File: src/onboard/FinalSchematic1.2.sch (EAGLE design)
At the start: 81 parts, among them IC1 MIC29310-5.0BT, IC3 A5975D

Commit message: Removed old baro
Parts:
- removed BAROMETER: (no value), con-lstb:MA04-1
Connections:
- net 5V: no longer BAROMETER.1
- net GND: no longer BAROMETER.2
- net SCL: no longer BAROMETER.4
- net SDA: no longer BAROMETER.3
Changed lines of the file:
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@@
 <part name="GPSMTK3339" library="AERO_Eagle_Library" deviceset="ADAFRUIT_MTK3339_GPS" device=""/>
 <part name="RADIO" library="AERO_Eagle_Library" deviceset="ADAFRUIT_RFM95W_LORA_RADIO" device=""/>
-<part name="BAROMETER" library="con-lstb" library_urn="urn:adsk.eagle:library:162" deviceset="MA04-1" device="" package3d_urn="urn:adsk.eagle:package:8337/1"/>
 <part name="SERVO_DRIVER" library="PCA9685PW_112" deviceset="PCA9685PW,112" device=""/>
 <part name="GND2" library="supply1" library_urn="urn:adsk.eagle:library:371" deviceset="GND" device=""/>
@@
 <instance part="GPSMTK3339" gate="G$1" x="48.26" y="80.01" smashed="yes" rot="R270"/>
 <instance part="RADIO" gate="G$1" x="96.52" y="78.74" smashed="yes" rot="R270"/>
-<instance part="BAROMETER" gate="1" x="-2.54" y="58.42" smashed="yes" rot="R180">
-<attribute name="VALUE" x="-1.27" y="68.58" size="1.778" layer="96" rot="R180"/>
-<attribute name="NAME" x="-1.27" y="52.578" size="1.778" layer="95" rot="R180"/>
-</instance>
 <instance part="IMU" gate="G$1" x="144.78" y="35.56" smashed="yes" rot="R270"/>
 <instance part="R32" gate="G$1" x="76.2" y="5.08" smashed="yes" rot="R90">
@@
 </segment>
 <segment>
-<pinref part="BAROMETER" gate="1" pin="1"/>
-<wire x1="-10.16" y1="63.5" x2="-12.7" y2="63.5" width="0.1524" layer="91"/>
-<label x="-17.78" y="63.5" size="1.778" layer="95"/>
-</segment>
-<segment>
 <pinref part="RADIO" gate="G$1" pin="VIN"/>
 <wire x1="91.44" y1="73.66" x2="87.63" y2="73.66" width="0.1524" layer="91"/>
@@
 </segment>
 <segment>
-<pinref part="BAROMETER" gate="1" pin="3"/>
-<wire x1="-10.16" y1="58.42" x2="-12.7" y2="58.42" width="0.1524" layer="91"/>
-<label x="-17.78" y="58.42" size="1.778" layer="95"/>
-</segment>
-<segment>
 <pinref part="R33" gate="G$1" pin="1"/>
 <wire x1="66.04" y1="0" x2="66.04" y2="-2.54" width="0.1524" layer="91"/>
@@
 </segment>
 <segment>
-<pinref part="BAROMETER" gate="1" pin="4"/>
-<wire x1="-10.16" y1="55.88" x2="-12.7" y2="55.88" width="0.1524" layer="91"/>
-<label x="-17.78" y="55.88" size="1.778" layer="95"/>
-</segment>
-<segment>
 <pinref part="R32" gate="G$1" pin="1"/>
 <wire x1="76.2" y1="0" x2="76.2" y2="-2.54" width="0.1524" layer="91"/>
@@
 </segment>
 <segment>
-<pinref part="BAROMETER" gate="1" pin="2"/>
-<wire x1="-10.16" y1="60.96" x2="-12.7" y2="60.96" width="0.1524" layer="91"/>
-<label x="-17.78" y="60.96" size="1.778" layer="95"/>
-</segment>
-<segment>

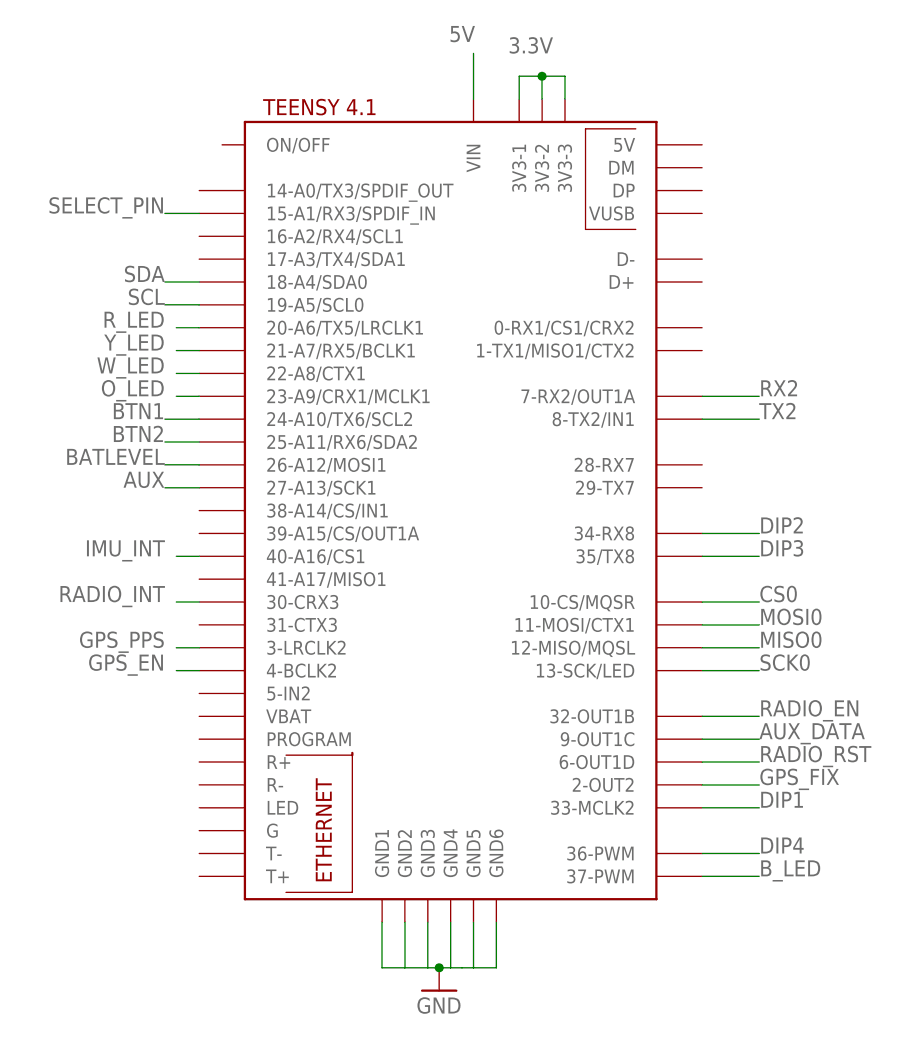
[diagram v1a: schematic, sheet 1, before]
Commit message: Rewired pins for easier routing
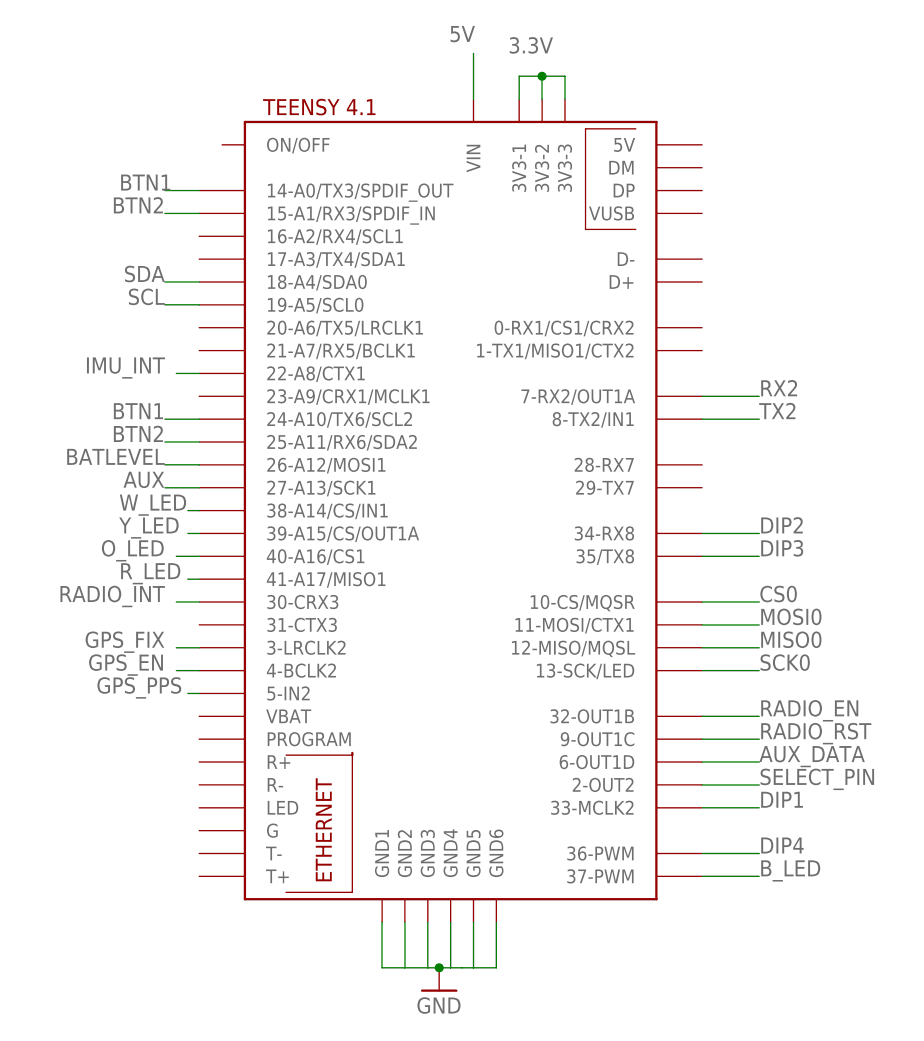
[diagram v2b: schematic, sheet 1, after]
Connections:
- net AUX_DATA: now also TEENSY4.1.6-OUT1D; no longer TEENSY4.1.9-OUT1C
- net BTN1: now also TEENSY4.1.14-A0/TX3/SPDIF_OUT
- net BTN2: now also TEENSY4.1.15-A1/RX3/SPDIF_IN
- net GPS_FIX: now also TEENSY4.1.3-LRCLK2; no longer TEENSY4.1.2-OUT2
- net GPS_PPS: now also TEENSY4.1.5-IN2; no longer TEENSY4.1.3-LRCLK2
- net IMU_INT: now also TEENSY4.1.22-A8/CTX1; no longer TEENSY4.1.40-A16/CS1
- net O_LED: now also TEENSY4.1.40-A16/CS1; no longer TEENSY4.1.23-A9/CRX1/MCLK1
- net RADIO_RST: now also TEENSY4.1.9-OUT1C; no longer TEENSY4.1.6-OUT1D
- net R_LED: now also TEENSY4.1.41-A17/MISO1; no longer TEENSY4.1.20-A6/TX5/LRCLK1
- net SELECT_PIN: now also TEENSY4.1.2-OUT2; no longer TEENSY4.1.15-A1/RX3/SPDIF_IN
- net W_LED: now also TEENSY4.1.38-A14/CS/IN1; no longer TEENSY4.1.22-A8/CTX1
- net Y_LED: now also TEENSY4.1.39-A15/CS/OUT1A; no longer TEENSY4.1.21-A7/RX5/BCLK1
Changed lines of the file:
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@@
-</segment>
-</net>
-<net name="GPS_FIX" class="0">
-<segment>
-<pinref part="TEENSY4.1" gate="G$1" pin="2-OUT2"/>
-<wire x1="90.17" y1="15.24" x2="96.52" y2="15.24" width="0.1524" layer="91"/>
-<label x="96.52" y="15.24" size="1.778" layer="95"/>
 </segment>
 </net>
 <net name="GPS_PPS" class="0">
 <segment>
-<pinref part="TEENSY4.1" gate="G$1" pin="3-LRCLK2"/>
-<wire x1="34.29" y1="30.48" x2="31.75" y2="30.48" width="0.1524" layer="91"/>
-<label x="30.48" y="30.48" size="1.778" layer="95" align="bottom-right"/>
+<pinref part="TEENSY4.1" gate="G$1" pin="5-IN2"/>
+<wire x1="34.29" y1="25.4" x2="33.02" y2="25.4" width="0.1524" layer="91"/>
+<label x="22.86" y="25.4" size="1.778" layer="95"/>
 </segment>
 </net>
@@
 <wire x1="34.29" y1="35.56" x2="31.75" y2="35.56" width="0.1524" layer="91"/>
 <label x="30.48" y="35.56" size="1.778" layer="95" align="bottom-right"/>
-</segment>
-</net>
-<net name="RADIO_RST" class="0">
-<segment>
-<pinref part="TEENSY4.1" gate="G$1" pin="6-OUT1D"/>
-<wire x1="90.17" y1="17.78" x2="96.52" y2="17.78" width="0.1524" layer="91"/>
-<label x="96.52" y="17.78" size="1.778" layer="95"/>
 </segment>
 </net>
@@
 <net name="IMU_INT" class="0">
 <segment>
-<pinref part="TEENSY4.1" gate="G$1" pin="40-A16/CS1"/>
-<wire x1="34.29" y1="40.64" x2="31.75" y2="40.64" width="0.1524" layer="91"/>
-<label x="30.48" y="40.64" size="1.778" layer="95" align="bottom-right"/>
-</segment>
-</net>
-<net name="W_LED" class="0">
-<segment>
 <pinref part="TEENSY4.1" gate="G$1" pin="22-A8/CTX1"/>
 <wire x1="34.29" y1="60.96" x2="31.75" y2="60.96" width="0.1524" layer="91"/>
 <label x="30.48" y="60.96" size="1.778" layer="95" align="bottom-right"/>
-</segment>
-</net>
-<net name="Y_LED" class="0">
-<segment>
-<pinref part="TEENSY4.1" gate="G$1" pin="21-A7/RX5/BCLK1"/>
-<wire x1="34.29" y1="63.5" x2="31.75" y2="63.5" width="0.1524" layer="91"/>
-<label x="30.48" y="63.5" size="1.778" layer="95" align="bottom-right"/>
-</segment>
-</net>
-<net name="R_LED" class="0">
-<segment>
-<pinref part="TEENSY4.1" gate="G$1" pin="20-A6/TX5/LRCLK1"/>
-<wire x1="34.29" y1="66.04" x2="31.75" y2="66.04" width="0.1524" layer="91"/>
-<label x="30.48" y="66.04" size="1.778" layer="95" align="bottom-right"/>
 </segment>
 </net>
@@
 <net name="AUX_DATA" class="0">
 <segment>
-<pinref part="TEENSY4.1" gate="G$1" pin="9-OUT1C"/>
-<wire x1="90.17" y1="20.32" x2="96.52" y2="20.32" width="0.1524" layer="91"/>
-<label x="96.52" y="20.32" size="1.778" layer="95"/>
-</segment>
-</net>
-<net name="SELECT_PIN" class="0">
-<segment>
-<pinref part="TEENSY4.1" gate="G$1" pin="15-A1/RX3/SPDIF_IN"/>
-<wire x1="34.29" y1="78.74" x2="30.48" y2="78.74" width="0.1524" layer="91"/>
-<label x="30.48" y="78.74" size="1.778" layer="95" align="bottom-right"/>
-</segment>
-</net>
-<net name="O_LED" class="0">
-<segment>
-<pinref part="TEENSY4.1" gate="G$1" pin="23-A9/CRX1/MCLK1"/>
-<wire x1="34.29" y1="58.42" x2="31.75" y2="58.42" width="0.1524" layer="91"/>
-<label x="30.48" y="58.42" size="1.778" layer="95" align="bottom-right"/>
+<pinref part="TEENSY4.1" gate="G$1" pin="6-OUT1D"/>
+<wire x1="90.17" y1="17.78" x2="96.52" y2="17.78" width="0.1524" layer="91"/>
+<label x="96.52" y="17.78" size="1.778" layer="95"/>
 </segment>
 </net>
@@
 <label x="30.48" y="53.34" size="1.778" layer="95" align="bottom-right"/>
 </segment>
+<segment>
+<pinref part="TEENSY4.1" gate="G$1" pin="15-A1/RX3/SPDIF_IN"/>
+<wire x1="34.29" y1="78.74" x2="30.48" y2="78.74" width="0.1524" layer="91"/>
+<label x="30.48" y="78.74" size="1.778" layer="95" align="bottom-right"/>
+</segment>
 </net>
 <net name="BTN1" class="0">
@@
 <wire x1="34.29" y1="55.88" x2="30.48" y2="55.88" width="0.1524" layer="91"/>
 <label x="30.48" y="55.88" size="1.778" layer="95" align="bottom-right"/>
+</segment>
+<segment>
+<pinref part="TEENSY4.1" gate="G$1" pin="14-A0/TX3/SPDIF_OUT"/>
+<wire x1="34.29" y1="81.28" x2="30.48" y2="81.28" width="0.1524" layer="91"/>
+<label x="25.4" y="81.28" size="1.778" layer="95"/>
 </segment>
 </net>
@@
 </segment>
 </net>
+<net name="RADIO_RST" class="0">
+<segment>
+<pinref part="TEENSY4.1" gate="G$1" pin="9-OUT1C"/>
+<wire x1="90.17" y1="20.32" x2="96.52" y2="20.32" width="0.1524" layer="91"/>
+<label x="96.52" y="20.32" size="1.778" layer="95"/>
+</segment>
+</net>
+<net name="W_LED" class="0">
+<segment>
+<pinref part="TEENSY4.1" gate="G$1" pin="38-A14/CS/IN1"/>
+<wire x1="34.29" y1="45.72" x2="33.02" y2="45.72" width="0.1524" layer="91"/>
+<label x="25.4" y="45.72" size="1.778" layer="95"/>
+</segment>
+</net>
+<net name="Y_LED" class="0">
+<segment>
+<pinref part="TEENSY4.1" gate="G$1" pin="39-A15/CS/OUT1A"/>
+<wire x1="34.29" y1="43.18" x2="33.02" y2="43.18" width="0.1524" layer="91"/>
+<label x="25.4" y="43.18" size="1.778" layer="95"/>
+</segment>
+</net>
+<net name="O_LED" class="0">
+<segment>
+<pinref part="TEENSY4.1" gate="G$1" pin="40-A16/CS1"/>
+<wire x1="34.29" y1="40.64" x2="31.75" y2="40.64" width="0.1524" layer="91"/>
+<label x="30.48" y="40.64" size="1.778" layer="95" align="bottom-right"/>
+</segment>
+</net>
+<net name="R_LED" class="0">
+<segment>
+<pinref part="TEENSY4.1" gate="G$1" pin="41-A17/MISO1"/>
+<wire x1="34.29" y1="38.1" x2="33.02" y2="38.1" width="0.1524" layer="91"/>
+<label x="25.4" y="38.1" size="1.778" layer="95"/>
+</segment>
+</net>
+<net name="SELECT_PIN" class="0">
+<segment>
+<pinref part="TEENSY4.1" gate="G$1" pin="2-OUT2"/>
+<wire x1="90.17" y1="15.24" x2="96.52" y2="15.24" width="0.1524" layer="91"/>
+<label x="96.52" y="15.24" size="1.778" layer="95"/>
+</segment>
+</net>
+<net name="GPS_FIX" class="0">
+<segment>
+<pinref part="TEENSY4.1" gate="G$1" pin="3-LRCLK2"/>
+<wire x1="34.29" y1="30.48" x2="31.75" y2="30.48" width="0.1524" layer="91"/>
+<label x="30.48" y="30.48" size="1.778" layer="95" align="bottom-right"/>
+</segment>
+</net>
